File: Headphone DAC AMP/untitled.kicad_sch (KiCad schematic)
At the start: 26 parts, among them Q1 PMOS, U10 TLV71x_WSON-6, U11 TPS65131RGE

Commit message: Power updated
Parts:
- added C35: 10n, symbol Device:C
- added R23: 90.9K, symbol Device:R
- added R24, R26: 10K, symbol Device:R
- added R25: 100K, symbol Device:R
- added U12: TPS7A3901DSCR, TPS7A3901DSCR:SON50P300X300X80-11N, symbol TPS7A3901DSCR:TPS7A3901DSCR
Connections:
- net GND: now also U11.19 (AGND), U11.2 (PGND), U11.25 (EP), U11.3 (PGND), C35.2, R24.2, U12.11 (GND__1), U12.11_1 (GND__2), U12.11_2 (GND__3), U12.11_3 (GND__4), U12.11_4 (GND__5), U12.4 (GND)
- net VBUS: now reaches C33.1, Q1.3 (S), R21.1, U11.5 (INN), U11.6 (INN)
- net +12V_PreFLT: now reaches C26.1, C27.1, D1.1 (K), R18.1, U11.23 (VPOS)
- net +12V_PreFLT: now also U12.1 (INP)
- net -12V_PreFLT: now reaches C29.2, C32.2, D3.2 (A), R20.2, U11.15 (VNEG)
- net -12V_PreFLT: now also U12.5 (INN)
- new net: C35.1, U12.3 (NR/SS)
- new net: R26.2, U12.8 (BUF)
- new net +12V_FLT: R23.1, U12.10 (OUTP)
- new net -12V_FLT: R25.1, U12.6 (OUTN)
- new net FB+12: R23.2, R24.1, U12.9 (FBP)
- new net FB-12: R25.2, R26.1, U12.7 (FBN)

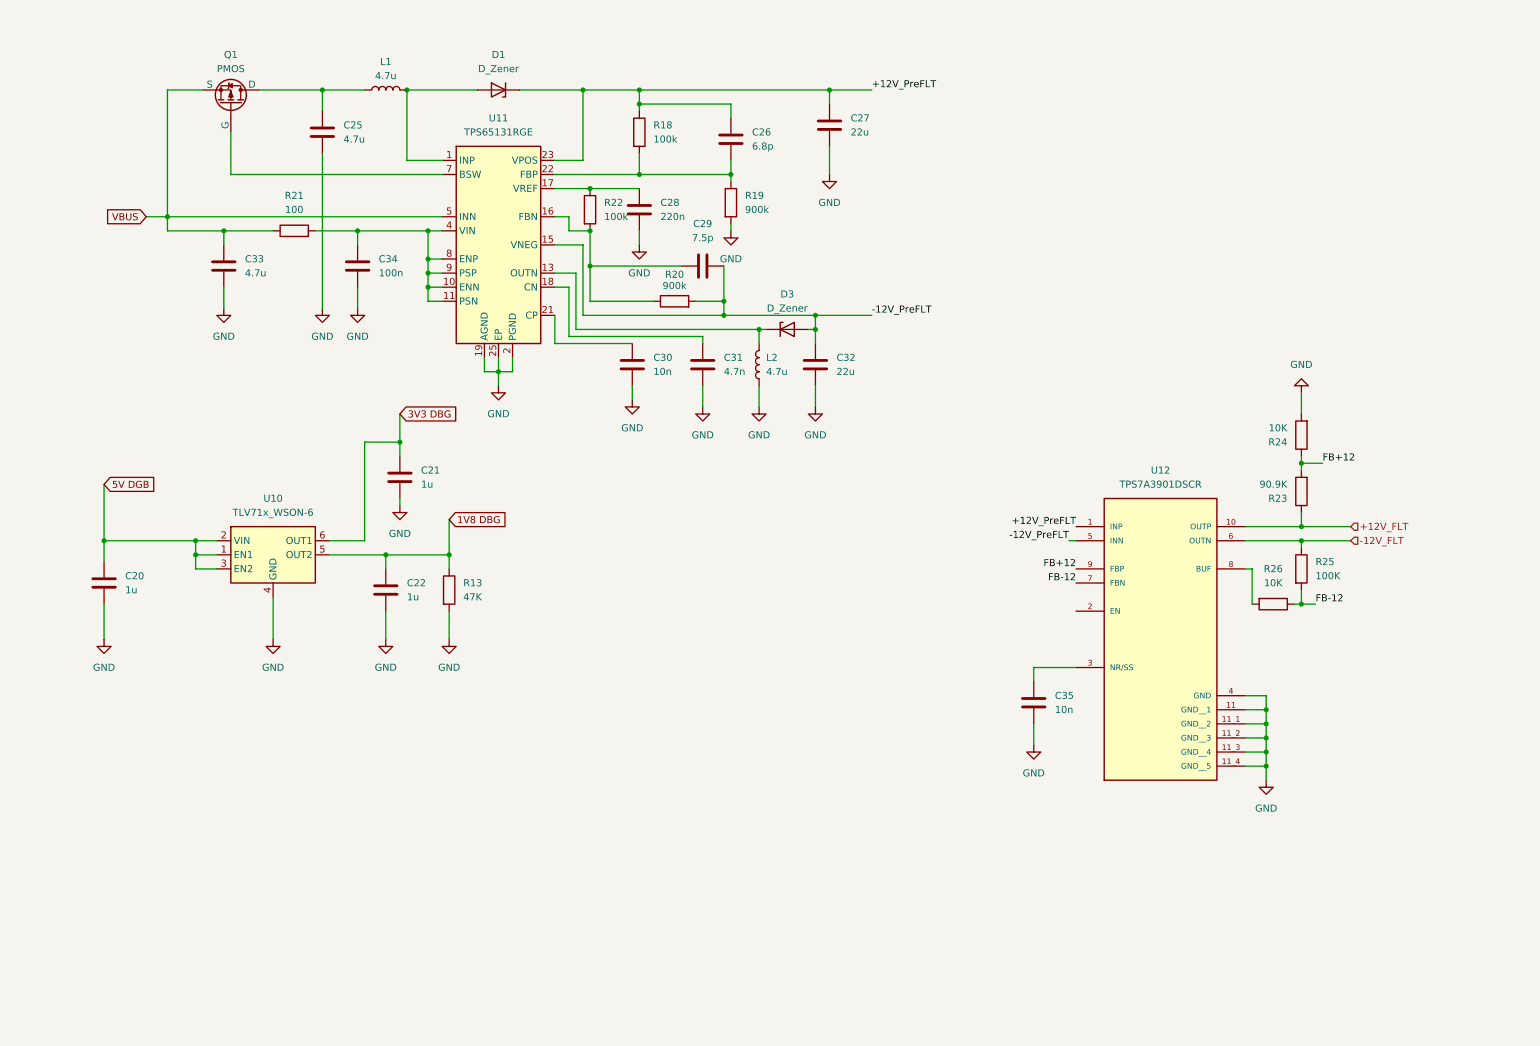
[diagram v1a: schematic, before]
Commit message: Added +-5V Regulator
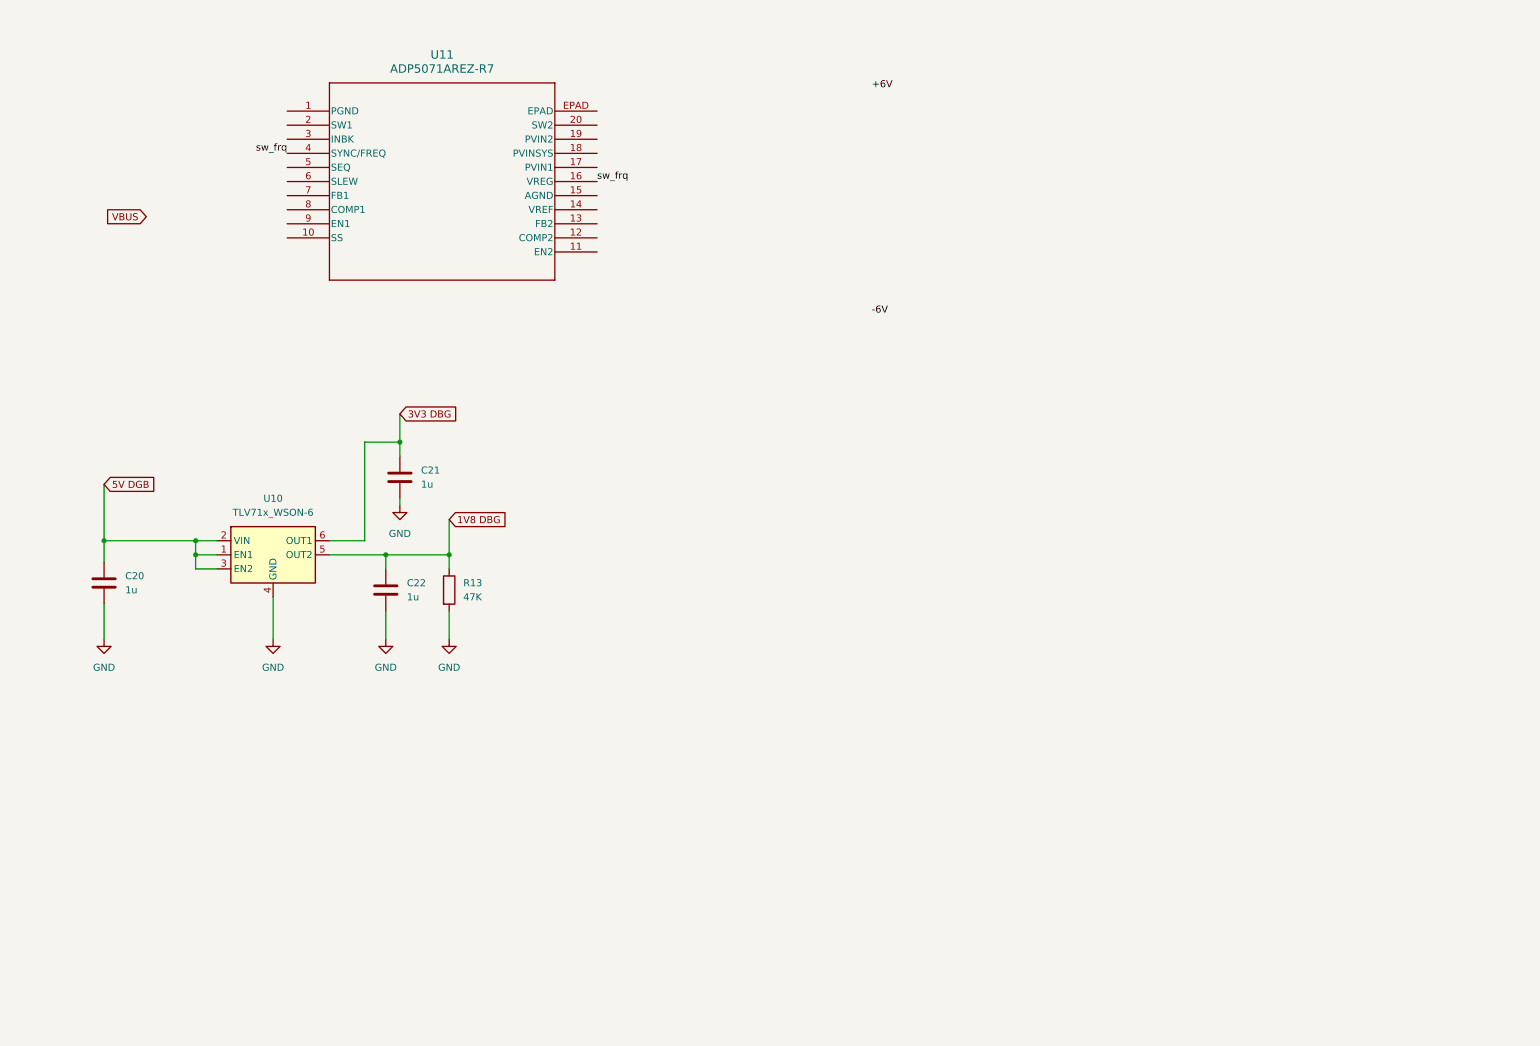
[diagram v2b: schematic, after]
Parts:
- removed C25, C33: 4.7u, symbol Device:C
- removed C26: 6.8p, symbol Device:C
- removed C27, C32: 22u, symbol Device:C
- removed C28: 220n, symbol Device:C
- removed C29: 7.5p, symbol Device:C
- removed C30, C35: 10n, symbol Device:C
- removed C31: 4.7n, symbol Device:C
- removed C34: 100n, symbol Device:C
- removed D1, D3: D_Zener, symbol Device:D_Zener
- removed L1, L2: 4.7u, symbol Device:L
- removed Q1: PMOS, symbol Simulation_SPICE:PMOS
- removed R18, R22: 100k, symbol Device:R
- removed R19, R20: 900k, symbol Device:R
- removed R21: 100, symbol Device:R
- removed R23: 90.9K, symbol Device:R
- removed R24, R26: 10K, symbol Device:R
- removed R25: 100K, symbol Device:R
- removed U11: TPS65131RGE, Package_DFN_QFN:VQFN-24-1EP_4x4mm_P0.5mm_EP2.45x2.45mm_ThermalVias, symbol Regulator_Switching:TPS65131RGE
- removed U12: TPS7A3901DSCR, TPS7A3901DSCR:SON50P300X300X80-11N, symbol TPS7A3901DSCR:TPS7A3901DSCR
- added U11: ADP5071AREZ-R7, RE-20-1_ADI, symbol ADP5071AREZ-R7:ADP5071AREZ-R7
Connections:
- new net sw_frq: U11.16 (VREG), U11.4 (SYNC/FREQ)

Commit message: Added +-5v filtered output
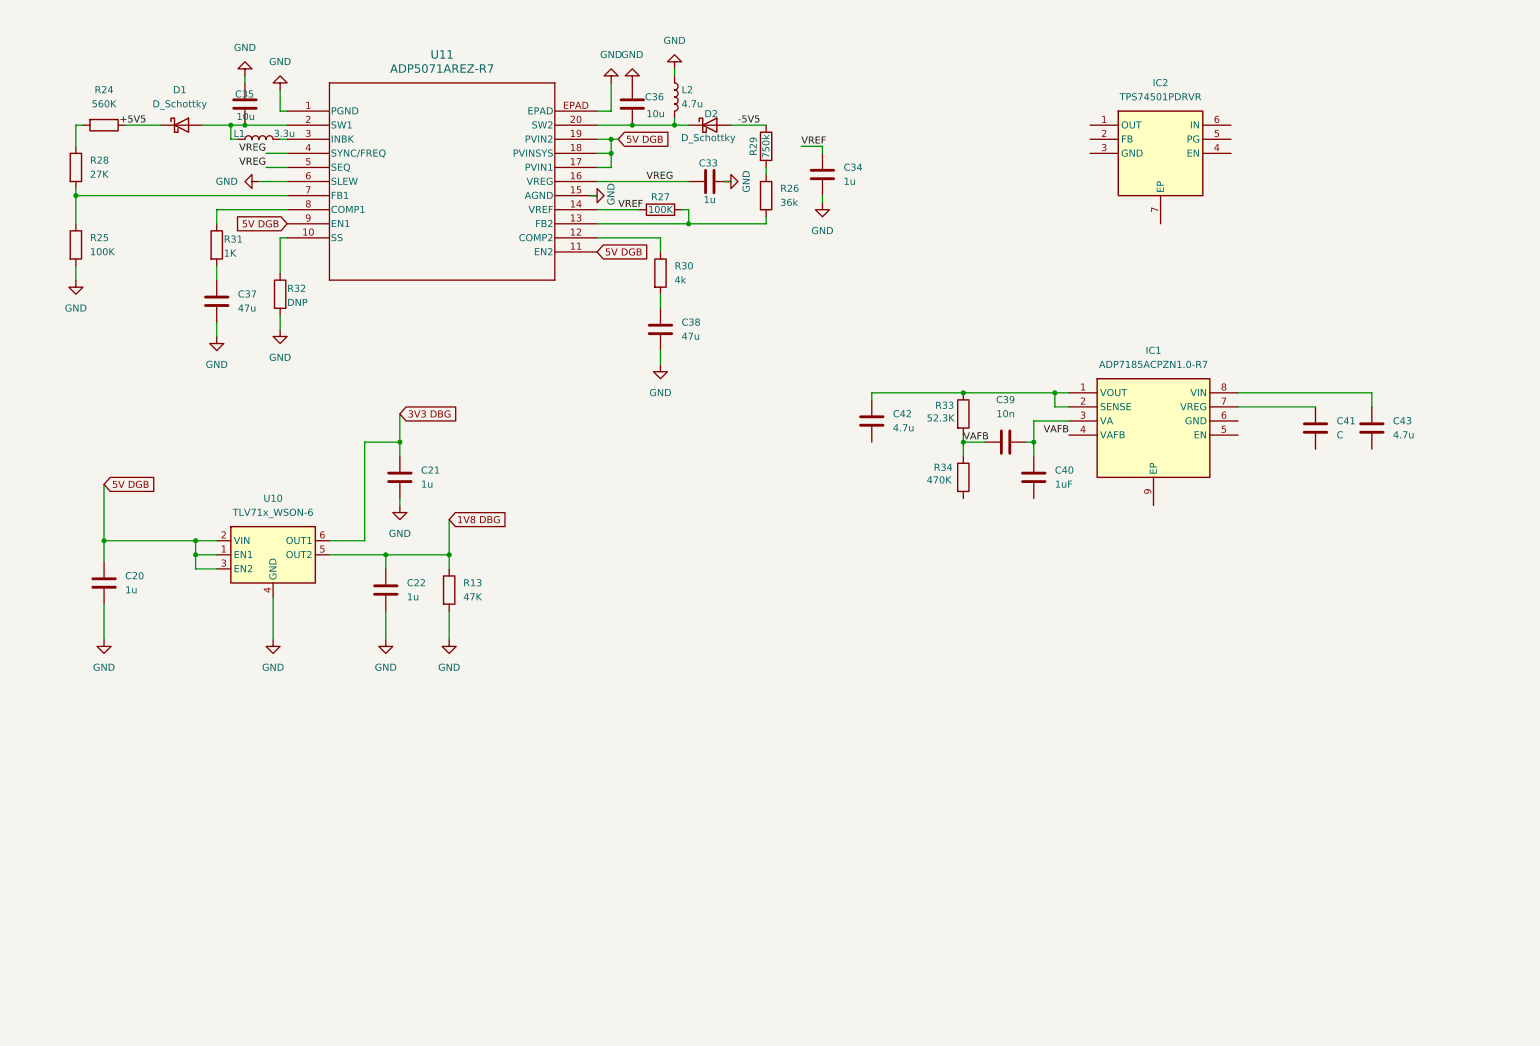
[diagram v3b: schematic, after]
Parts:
- added C33, C34: 1u, symbol Device:C
- added C35, C36: 10u, symbol Device:C
- added C37, C38: 47u, symbol Device:C
- added C39: 10n, symbol Device:C
- added C40: 1uF, symbol Device:C
- added C41: C, symbol Device:C
- added C42, C43: 4.7u, symbol Device:C
- added D1, D2: D_Schottky, symbol Device:D_Schottky
- added IC1: ADP7185ACPZN1.0-R7, SON50P200X200X60-9N, symbol ADP7185ACPZN1_0-R7:ADP7185ACPZN1.0-R7
- added IC2: TPS74501PDRVR, SON65P200X200X80-7N, symbol TPS74501PDRVR:TPS74501PDRVR
- added L1: 3.3u, symbol Device:L
- added L2: 4.7u, symbol Device:L
- added R24: 560K, symbol Device:R
- added R25, R27: 100K, symbol Device:R
- added R26: 36k, symbol Device:R
- added R28: 27K, symbol Device:R
- added R29: 750k, symbol Device:R
- added R30: 4k, symbol Device:R
- added R31: 1K, symbol Device:R
- added R32: DNP, symbol Device:R
- added R33: 52.3K, symbol Device:R
- added R34: 470K, symbol Device:R
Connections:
- net sw_frq is gone; now on net VREG: U11.16 (VREG), U11.4 (SYNC/FREQ)
- net 5V DGB: now also U11.11 (EN2), U11.17 (PVIN1), U11.18 (PVINSYS), U11.19 (PVIN2), U11.9 (EN1)
- net GND: now also U11.1 (PGND), U11.15 (AGND), U11.6 (SLEW), U11.EPAD, C33.2, C34.2, C35.1, C36.1, C37.2, C38.2, L2.1, R25.2, R32.2
- net at U11.10 (SS): now also R32.1
- net at U11.12 (COMP2): now also R30.1
- net at U11.13 (FB2): now also R26.2, R27.2
- net VREF: now reaches U11.14 (VREF)
- net VREF: now also C34.1, R27.1
- net at U11.2 (SW1): now also C35.2, D1.2 (A), L1.1
- net at U11.20 (SW2): now also C36.2, D2.1 (K), L2.2
- net at U11.3 (INBK): now also L1.2
- net VREG: now reaches U11.5 (SEQ)
- net VREG: now also C33.1
- net at U11.7 (FB1): now also R25.1, R28.2
- net at U11.8 (COMP1): now also R31.1
- new net: C37.1, R31.2
- new net: C39.2, C40.1, IC1.3 (VA)
- new net: C38.1, R30.2
- new net: C42.1, IC1.1 (VOUT), IC1.2 (SENSE), R33.1
- new net: R26.1, R29.2
- new net: C43.1, IC1.8 (VIN)
- new net: C41.1, IC1.7 (VREG)
- new net: R24.2, R28.1
- new net +5V5: D1.1 (K), R24.1
- new net -5V5: D2.2 (A), R29.1
- new net VAFB: C39.1, IC1.4 (VAFB), R33.2, R34.1
